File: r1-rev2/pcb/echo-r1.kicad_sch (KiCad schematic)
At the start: 76 parts, among them J2 TYPE-C-31-M-12, J3 TF-115, J6 PM254-1-06-W-8.5, J7 ILI9342C, Q4 AO3401A, SW1 POWER, SW10 DPAD→, SW11 START, SW12 SELECT, SW13 VOL+, SW14 VOL-, SW2 HOLD, SW3 A, SW4 B, SW5 X, SW6 Y, SW7 DPAD↑, SW8 DPAD↓, SW9 DPAD←, U7 STM32H7R3Z8Jx, U8 W958D8NBYA5I, Y1 SC-32S32.768kHz20PPM12.5pF, Y2 XTM32024000JT00351001

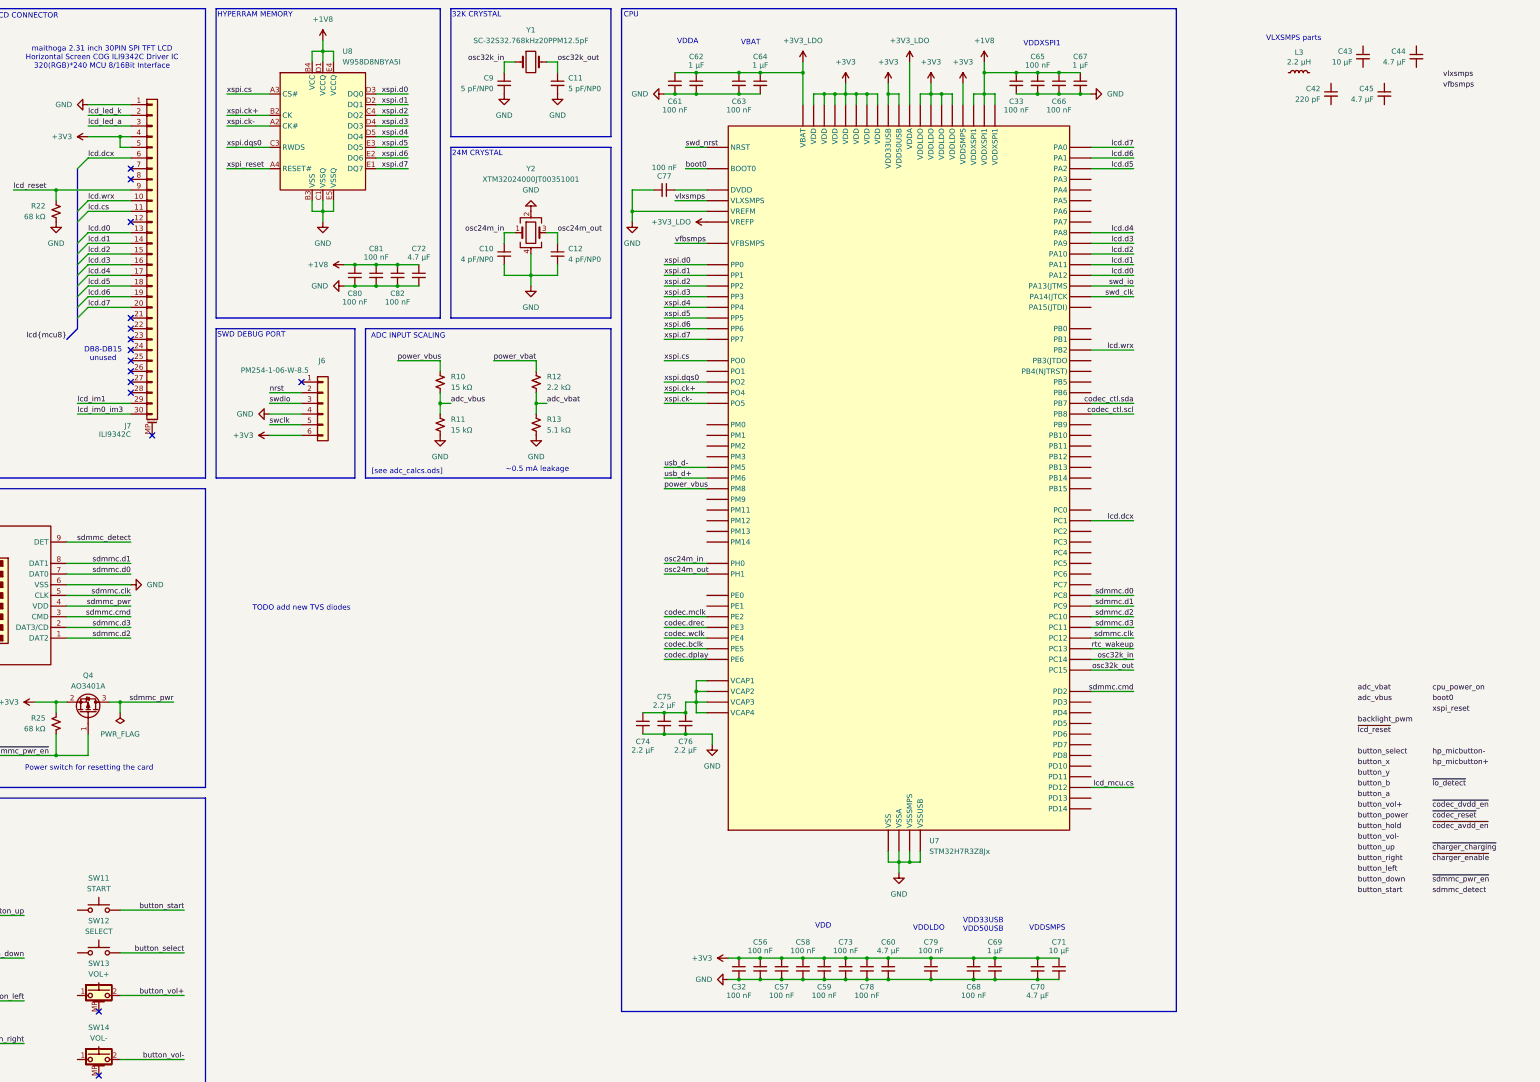
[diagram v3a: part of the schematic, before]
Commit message: R1-Rev2: finish STM32 power supply
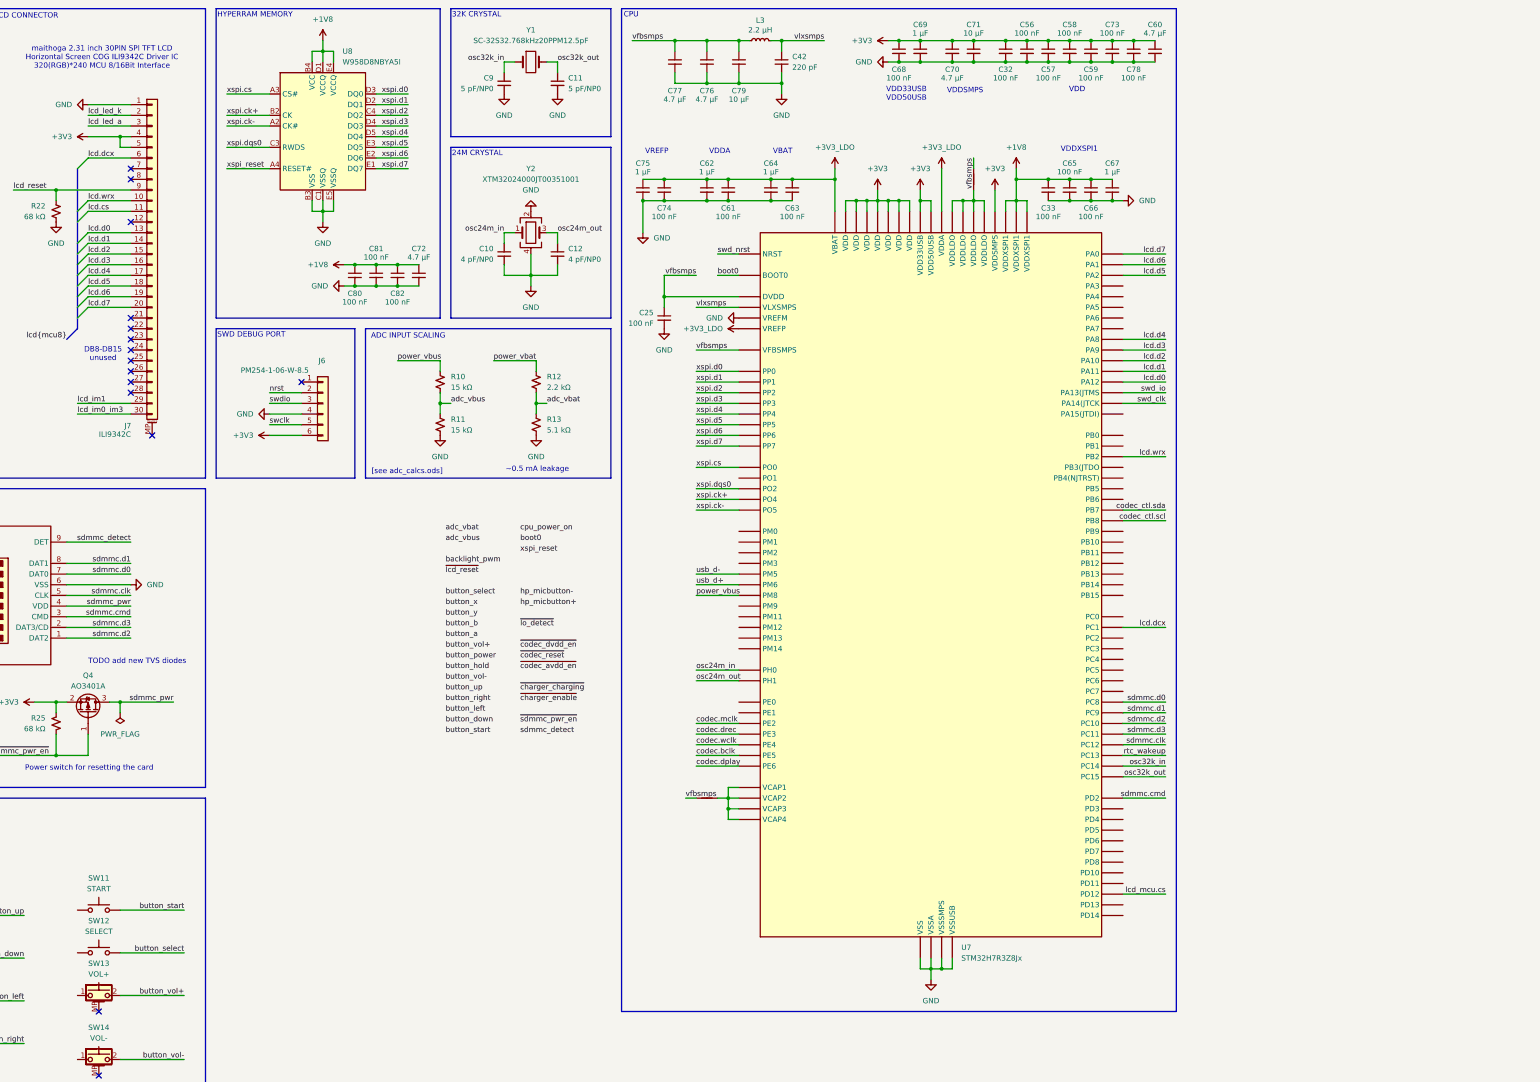
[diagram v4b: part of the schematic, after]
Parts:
- removed C43: 10 µF, Capacitor_SMD:C_0402_1005Metric, symbol Device:C_Small
- removed C44, C45: 4.7 µF, Capacitor_SMD:C_0402_1005Metric, symbol Device:C_Small
- added C25: 100 nF, Capacitor_SMD:C_0603_1608Metric, symbol Device:C_Small
- added NT3, NT4: NetTie_2, symbol Device:NetTie_2
- C74: value 2.2 µF -> 100 nF
- C75: value 2.2 µF -> 1 µF
- C76: value 2.2 µF -> 4.7 µF
- C77: value 100 nF -> 4.7 µF
- C79: value 100 nF -> 10 µF
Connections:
- net +3V3: no longer C79.1, U7.F6 (VDDLDO), U7.F7 (VDDLDO), U7.G6 (VDDLDO), U7.G7 (VDDLDO)
- net +3V3_LDO: now also C74.1, C75.1
- net GND: now also C42.2, C25.2
- net vfbsmps: now also C76.1, C77.1, C79.1, L3.1, U7.C8 (DVDD), C25.1, NT3.1, NT4.1
- net vlxsmps: now also C42.1, L3.2
- net at U7.E5 (VCAP4), U7.F8 (VCAP3), U7.H6 (VCAP1)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: now also NT3.2; no longer C74.1, C75.1, C76.1
- new net: NT4.2, U7.F6 (VDDLDO), U7.F7 (VDDLDO), U7.G6 (VDDLDO), U7.G7 (VDDLDO)
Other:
- note added: "VREFP"
- note removed: "VDDLDO"
- note removed: "VLXSMPS parts"
- moved on the sheet: C32, C33, C42, C56, C57, C58, C59, C60, C61, C62, C63, C64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

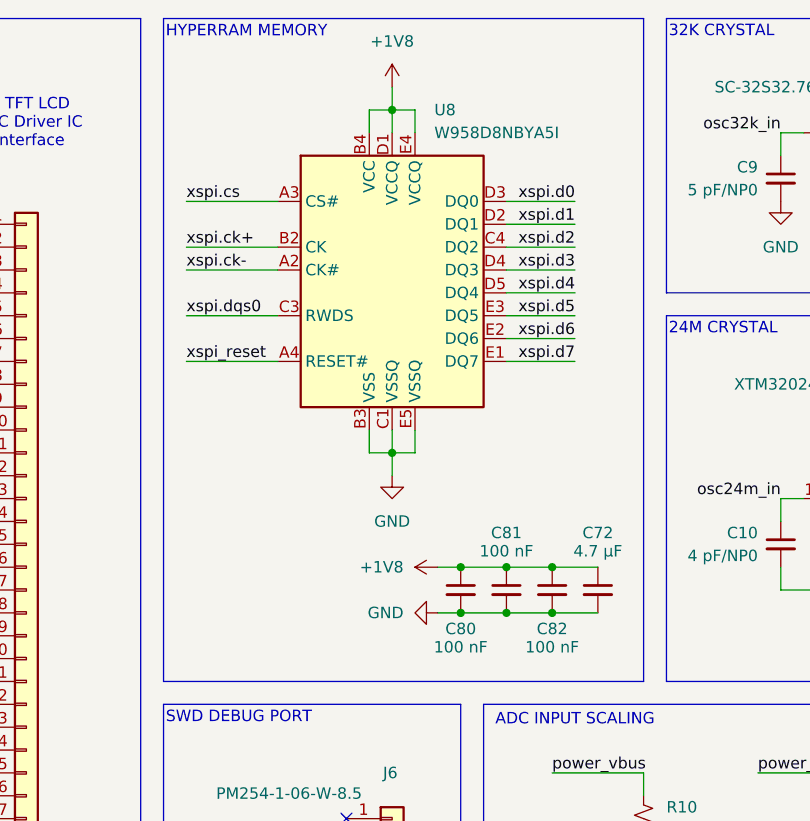
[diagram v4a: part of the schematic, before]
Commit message: R1-Rev2: remove bulk capacitor on RAM side of memory bus
There is already a 1 uF on the STM32 side, having extra bulk
capacitance is probably unnecessary considering the chips will
be placed very close to each other.
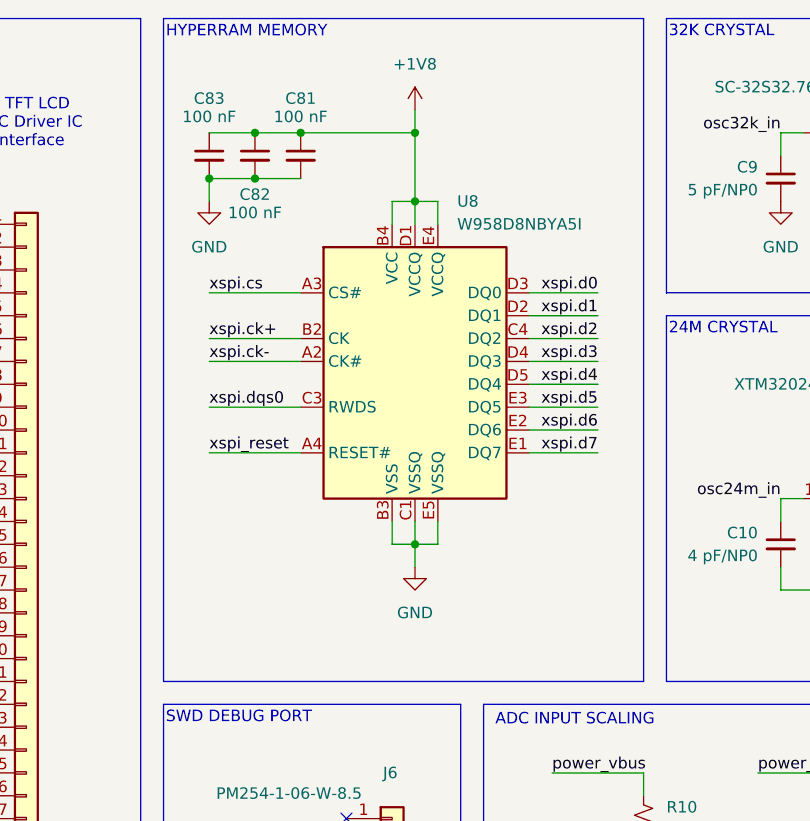
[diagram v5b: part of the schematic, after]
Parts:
- removed C72: 4.7 µF, Capacitor_SMD:C_0402_1005Metric, symbol Device:C_Small
- removed C80: 100 nF, Capacitor_SMD:C_0402_1005Metric, symbol Device:C_Small
- added C83: 100 nF, Capacitor_SMD:C_0402_1005Metric, symbol Device:C_Small
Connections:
- net +1V8: now also C83.1
- net GND: now also C83.2
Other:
- moved on the sheet: C81, C82, U8

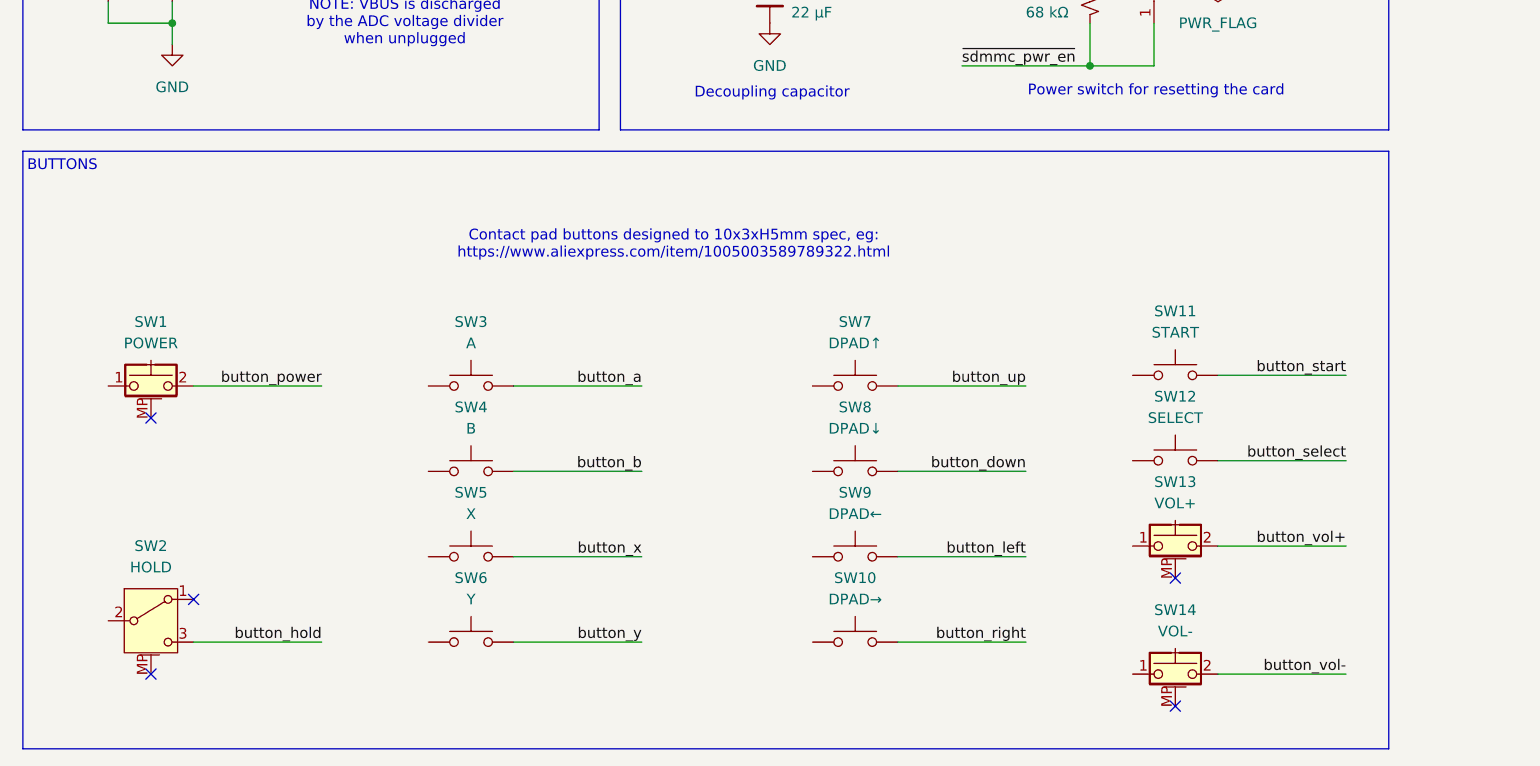
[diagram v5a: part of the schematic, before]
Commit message: R1-Rev2: convert buttons to SMD metal dome switches
Rubber domes increase mechanical complexity since they need to
be aligned and supported in the case to prevent them from going
off-center, and they require a lot of vertical space (~5mm).
Domes are also an additional component that has to be sourced
separately.

In contrast, prepackaged metal dome switches are normal SMD parts
and can be sourced and assembled alongside electronic components.
They are also much, much thinner and mechanical design is simpler.
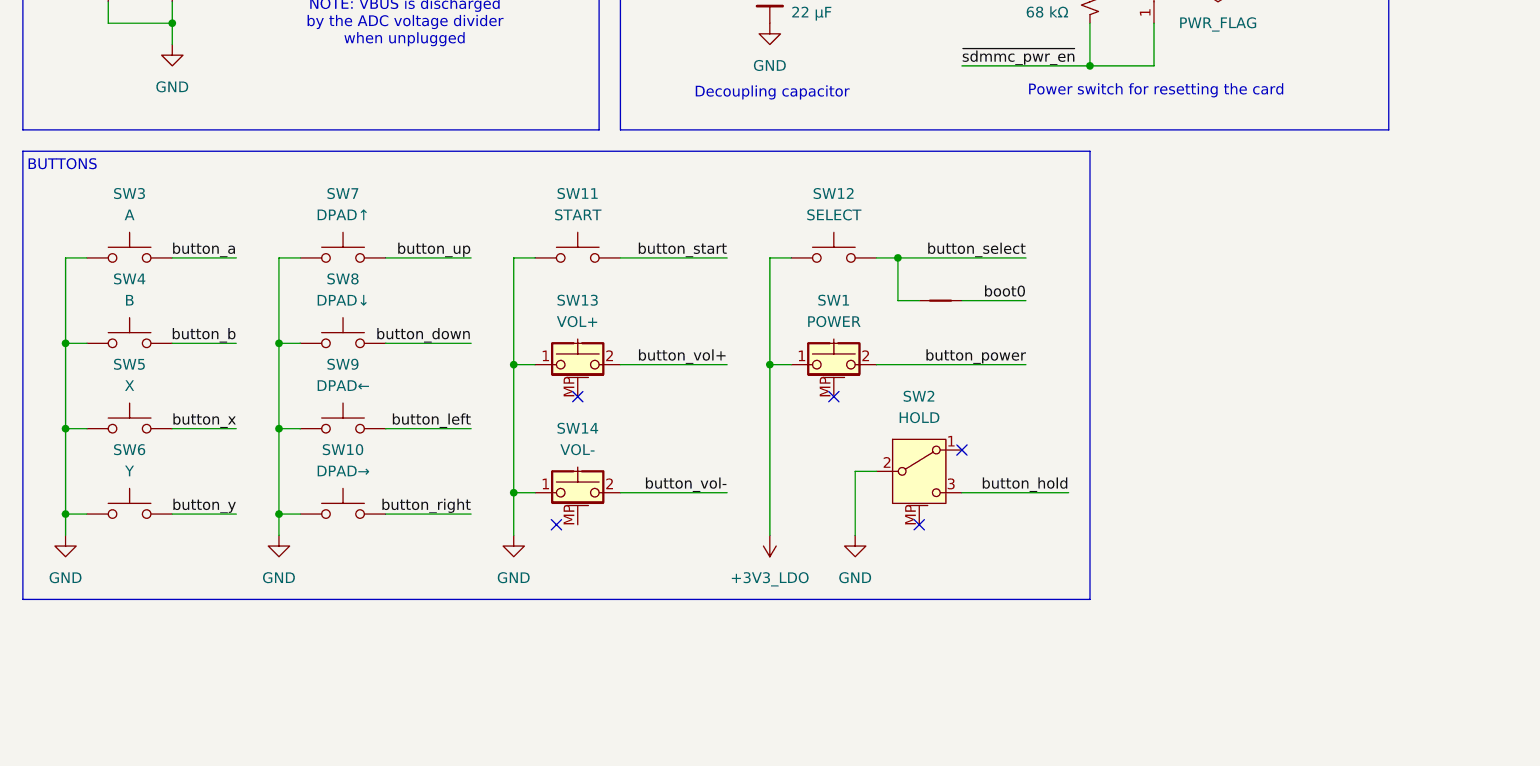
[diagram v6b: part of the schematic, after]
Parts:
- added NT5: NetTie_2, echoplayer:NetTie_0.15mm_SMD, symbol Device:NetTie_2
- SW10, SW3, SW4, SW5, SW6, SW7, SW8, SW9: footprint echoplayer:Switch_ContactPad_10x3mm_Cross -> echoplayer:Switch_SHOUHAN_TS3735PA
- SW11, SW12: footprint echoplayer:Switch_XUNPU_TS-1088-AR -> echoplayer:Switch_SHOUHAN_TS3735PA
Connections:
- net +3V3_LDO: now also SW1.1, SW12.1
- net GND: now also SW10.1, SW11.1, SW13.1, SW14.1, SW2.2 (B), SW3.1, SW4.1, SW5.1, SW6.1, SW7.1, SW8.1, SW9.1
- net boot0: now also NT5.2
- net button_select: now also NT5.1
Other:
- note removed: "Contact pad buttons designed to 10x3xH5mm spec, eg: https://www.aliexpress.com/item/1005003589789322.html"
- moved on the sheet: SW1, SW10, SW11, SW12, SW13, SW14, SW2, SW3, SW4, SW5, SW6, SW7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

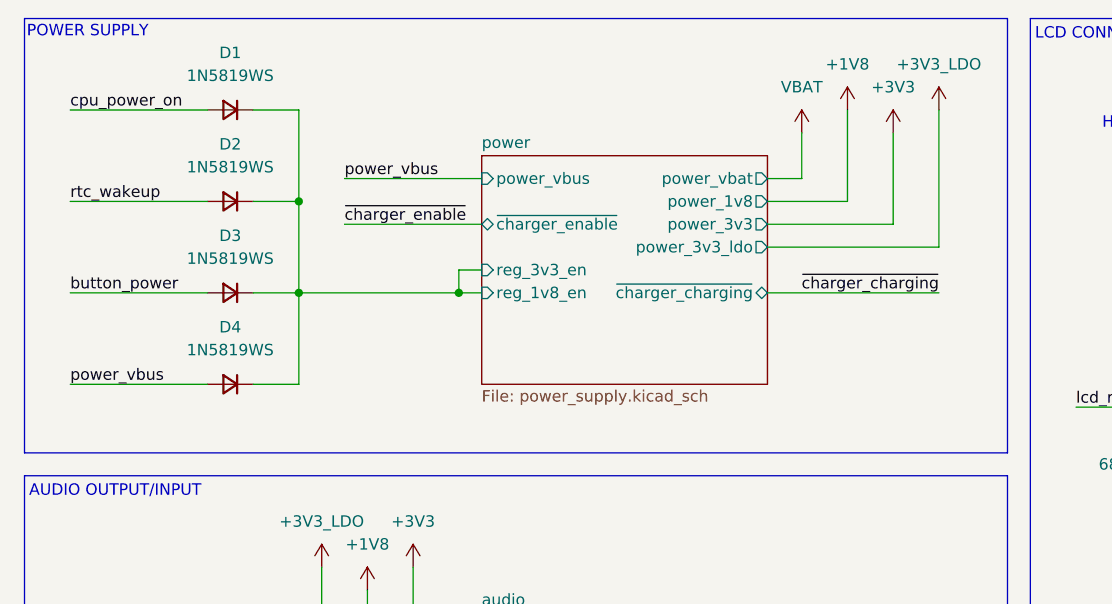
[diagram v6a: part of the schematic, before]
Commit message: R1-Rev2: add debouncing for regulator enable signal
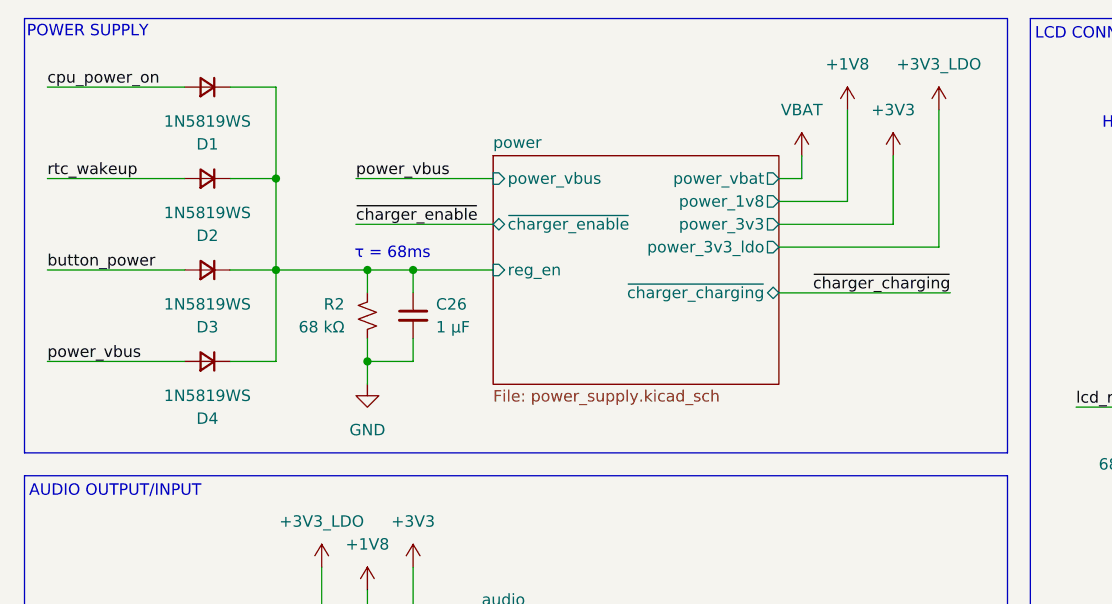
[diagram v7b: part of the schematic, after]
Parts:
- added C26: 1 µF, Capacitor_SMD:C_0805_2012Metric, symbol Device:C_Small
- added R2: 68 kΩ, Resistor_SMD:R_0402_1005Metric, symbol Device:R_Small_US
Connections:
- net GND: now also C26.2, R2.2
- net power/reg_1v8_en renamed power/reg_en
- net power/reg_en: now also C26.1, R2.1
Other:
- sheet power ports: added reg_en; removed reg_1v8_en, reg_3v3_en
- note added: "τ = 68ms"
- moved on the sheet: D1, D2, D3, D4
